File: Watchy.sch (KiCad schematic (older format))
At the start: 55 parts, among them J1 FPC24(0.5MM), J2 Micro USB, J3 Battery, M1 Vibration_Motor, Q1 AO3400A, Q2 UMH3N, Q4 CJ2301, Q5 S8050, SW1 BTN, SW2 BTN, SW3 BTN, SW4 BTN, U1 ESP32-PICO-D4, U2 ME6211C33M5G-N, U3 CP2104, U4 BMA423, U5 TP4054, U6 DS3231MZ

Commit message: added body step & STL
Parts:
- C1, C10, C11, C14, C2, C5, C6, C7, C8, C9: footprint Capacitors_SMD:C_0603 -> Capacitor_SMD:C_0603_1608Metric
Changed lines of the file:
@@
 F 0 "C1" H 865 1305 50  0000 L CNN
 F 1 "100nF" H 865 1235 50  0000 L CNN
-F 2 "Capacitors_SMD:C_0603" H 793 1090 50  0001 C CNN
+F 2 "Capacitor_SMD:C_0603_1608Metric" H 793 1090 50  0001 C CNN
 F 3 "" H 755 1240 50  0001 C CNN
 	1    755  1240
@@
 F 0 "C11" H 4890 4960 50  0000 L CNN
 F 1 "100nF" H 4890 4760 50  0000 L CNN
-F 2 "Capacitors_SMD:C_0603" H 4903 4710 50  0001 C CNN
+F 2 "Capacitor_SMD:C_0603_1608Metric" H 4903 4710 50  0001 C CNN
 F 3 "" H 4865 4860 50  0001 C CNN
 	1    4865 4860
@@
 F 0 "C2" V 9480 1545 50  0000 C CNN
 F 1 "1uF/50V" V 9645 1355 50  0000 C CNN
-F 2 "Capacitors_SMD:C_0603" H 9558 1305 50  0001 C CNN
+F 2 "Capacitor_SMD:C_0603_1608Metric" H 9558 1305 50  0001 C CNN
 F 3 "~" H 9520 1455 50  0001 C CNN
 	1    9520 1455
@@
 F 0 "C6" V 9555 2840 50  0000 C CNN
 F 1 "1uF/50V" V 9520 2155 50  0000 C CNN
-F 2 "Capacitors_SMD:C_0603" H 9558 2605 50  0001 C CNN
+F 2 "Capacitor_SMD:C_0603_1608Metric" H 9558 2605 50  0001 C CNN
 F 3 "~" H 9520 2755 50  0001 C CNN
 	1    9520 2755
@@
 F 0 "C8" V 9555 3040 50  0000 C CNN
 F 1 "1uF/50V" V 9525 2355 50  0000 C CNN
-F 2 "Capacitors_SMD:C_0603" H 9558 2805 50  0001 C CNN
+F 2 "Capacitor_SMD:C_0603_1608Metric" H 9558 2805 50  0001 C CNN
 F 3 "~" H 9520 2955 50  0001 C CNN
 	1    9520 2955
@@
 F 0 "C9" V 9555 3240 50  0000 C CNN
 F 1 "1uF/50V" V 9520 2540 50  0000 C CNN
-F 2 "Capacitors_SMD:C_0603" H 9558 3005 50  0001 C CNN
+F 2 "Capacitor_SMD:C_0603_1608Metric" H 9558 3005 50  0001 C CNN
 F 3 "~" H 9520 3155 50  0001 C CNN
 	1    9520 3155
@@
 F 0 "C10" V 9560 3470 50  0000 C CNN
 F 1 "1uF/50V" V 9520 2740 50  0000 C CNN
-F 2 "Capacitors_SMD:C_0603" H 9558 3205 50  0001 C CNN
+F 2 "Capacitor_SMD:C_0603_1608Metric" H 9558 3205 50  0001 C CNN
 F 3 "~" H 9520 3355 50  0001 C CNN
 	1    9520 3355
@@
 F 0 "C7" H 10540 2801 50  0000 L CNN
 F 1 "1uF/50V" H 10540 2710 50  0000 L CNN
-F 2 "Capacitors_SMD:C_0603" H 10463 2605 50  0001 C CNN
+F 2 "Capacitor_SMD:C_0603_1608Metric" H 10463 2605 50  0001 C CNN
 F 3 "~" H 10425 2755 50  0001 C CNN
 	1    10425 2755
@@
 F 0 "C5" H 7900 2060 50  0000 L CNN
 F 1 "1uF/50V" H 7900 1990 50  0000 L CNN
-F 2 "Capacitors_SMD:C_0603" H 7848 1920 50  0001 C CNN
+F 2 "Capacitor_SMD:C_0603_1608Metric" H 7848 1920 50  0001 C CNN
 F 3 "~" H 7810 2070 50  0001 C CNN
 	1    7810 2070
@@
 F 0 "C14" H 5735 7100 50  0000 L CNN
 F 1 "100nF" H 5860 6915 50  0000 L CNN
-F 2 "Capacitors_SMD:C_0603" H 5873 6870 50  0001 C CNN
+F 2 "Capacitor_SMD:C_0603_1608Metric" H 5873 6870 50  0001 C CNN
 F 3 "~" H 5835 7020 50  0001 C CNN
 	1    5835 7020

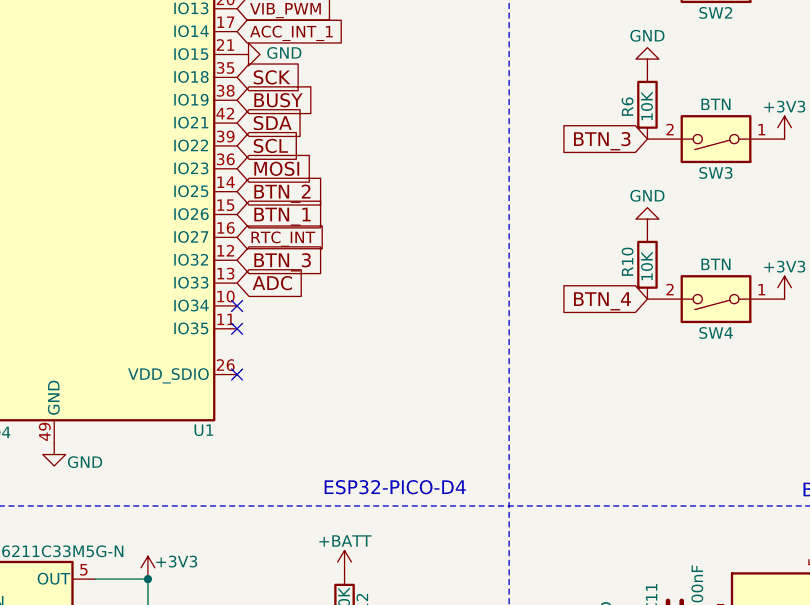
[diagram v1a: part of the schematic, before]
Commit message: added testpoints
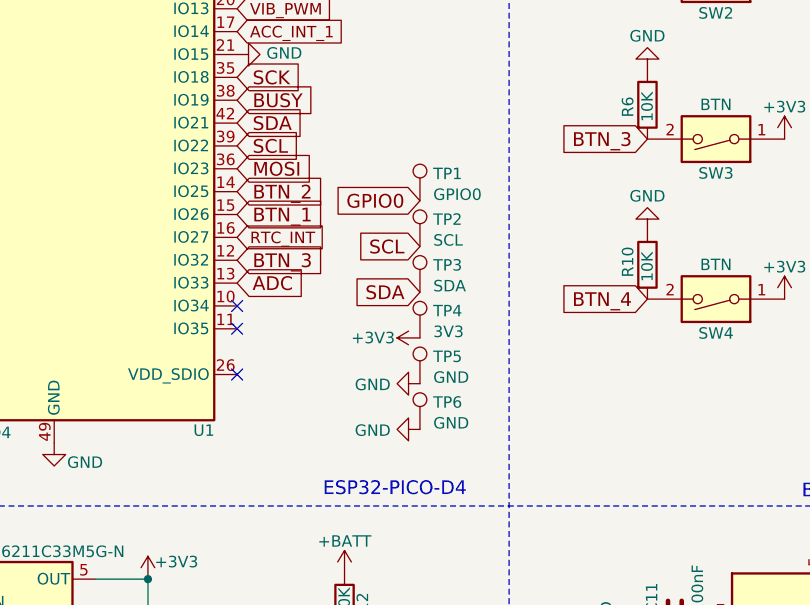
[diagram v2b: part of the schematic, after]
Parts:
- added TP1: GPIO0, TestPoint:TestPoint_Pad_D1.0mm, symbol Connector:TestPoint
- added TP2: SCL, TestPoint:TestPoint_Pad_D1.0mm, symbol Connector:TestPoint
- added TP3: SDA, TestPoint:TestPoint_Pad_D1.0mm, symbol Connector:TestPoint
- added TP4: 3V3, TestPoint:TestPoint_Pad_D1.0mm, symbol Connector:TestPoint
- added TP5, TP6: GND, TestPoint:TestPoint_Pad_D1.0mm, symbol Connector:TestPoint
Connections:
- net +3V3: now also TP4.1
- net GND: now also TP5.1, TP6.1
- net GPIO0: now also TP1.1
- net SCL: now also TP2.1
- net SDA: now also TP3.1
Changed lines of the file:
@@
 Wire Wire Line
 	9670 3255 9225 3255
+$Comp
+L Connector:TestPoint TP1
+U 1 1 60664F25
+P 3750 3030
+F 0 "TP1" H 3808 3148 50  0000 L CNN
+F 1 "GPIO0" H 3808 3057 50  0000 L CNN
+F 2 "TestPoint:TestPoint_Pad_D1.0mm" H 3950 3030 50  0001 C CNN
+F 3 "~" H 3950 3030 50  0001 C CNN
+	1    3750 3030
+	1    0    0    -1
+$EndComp
+$Comp
+L Connector:TestPoint TP2
+U 1 1 606661C8
+P 3750 3230
+F 0 "TP2" H 3808 3348 50  0000 L CNN
+F 1 "SCL" H 3808 3257 50  0000 L CNN
+F 2 "TestPoint:TestPoint_Pad_D1.0mm" H 3950 3230 50  0001 C CNN
+F 3 "~" H 3950 3230 50  0001 C CNN
+	1    3750 3230
+	1    0    0    -1
+$EndComp
+$Comp
+L Connector:TestPoint TP3
+U 1 1 60667C57
+P 3750 3430
+F 0 "TP3" H 3808 3548 50  0000 L CNN
+F 1 "SDA" H 3808 3457 50  0000 L CNN
+F 2 "TestPoint:TestPoint_Pad_D1.0mm" H 3950 3430 50  0001 C CNN
+F 3 "~" H 3950 3430 50  0001 C CNN
+	1    3750 3430
+	1    0    0    -1
+$EndComp
+$Comp
+L Connector:TestPoint TP4
+U 1 1 60668E1C
+P 3750 3630
+F 0 "TP4" H 3808 3748 50  0000 L CNN
+F 1 "3V3" H 3808 3657 50  0000 L CNN
+F 2 "TestPoint:TestPoint_Pad_D1.0mm" H 3950 3630 50  0001 C CNN
+F 3 "~" H 3950 3630 50  0001 C CNN
+	1    3750 3630
+	1    0    0    -1
+$EndComp
+$Comp
+L Connector:TestPoint TP5
+U 1 1 60669476
+P 3750 3830
+F 0 "TP5" H 3808 3948 50  0000 L CNN
+F 1 "GND" H 3808 3857 50  0000 L CNN
+F 2 "TestPoint:TestPoint_Pad_D1.0mm" H 3950 3830 50  0001 C CNN
+F 3 "~" H 3950 3830 50  0001 C CNN
+	1    3750 3830
+	1    0    0    -1
+$EndComp
+Text GLabel 3750 3030 0    60   Input ~ 0
+GPIO0
+Text GLabel 3750 3230 0    60   Input ~ 0
+SCL
+Text GLabel 3750 3430 0    60   Input ~ 0
+SDA
+$Comp
+L power:+3V3 #PWR0106
+U 1 1 60672CCA
+P 3750 3630
+F 0 "#PWR0106" H 3750 3480 50  0001 C CNN
+F 1 "+3V3" V 3750 3835 50  0000 C CNN
+F 2 "" H 3750 3630 50  0001 C CNN
+F 3 "" H 3750 3630 50  0001 C CNN
+	1    3750 3630
+	0    -1   -1   0
+$EndComp
+$Comp
+L power:GND #PWR0107
+U 1 1 60673AED
+P 3750 3830
+F 0 "#PWR0107" H 3750 3580 50  0001 C CNN
+F 1 "GND" V 3755 3702 50  0000 R CNN
+F 2 "" H 3750 3830 50  0001 C CNN
+F 3 "" H 3750 3830 50  0001 C CNN
+	1    3750 3830
+	0    1    1    0
+$EndComp
+$Comp
+L Connector:TestPoint TP6
+U 1 1 60739E66
+P 3750 4030
+F 0 "TP6" H 3808 4148 50  0000 L CNN
+F 1 "GND" H 3808 4057 50  0000 L CNN
+F 2 "TestPoint:TestPoint_Pad_D1.0mm" H 3950 4030 50  0001 C CNN
+F 3 "~" H 3950 4030 50  0001 C CNN
+	1    3750 4030
+	1    0    0    -1
+$EndComp
+$Comp
+L power:GND #PWR049
+U 1 1 6073A920
+P 3750 4030
+F 0 "#PWR049" H 3750 3780 50  0001 C CNN
+F 1 "GND" V 3755 3902 50  0000 R CNN
+F 2 "" H 3750 4030 50  0001 C CNN
+F 3 "" H 3750 4030 50  0001 C CNN
+	1    3750 4030
+	0    1    1    0
+$EndComp
 $EndSCHEMATC

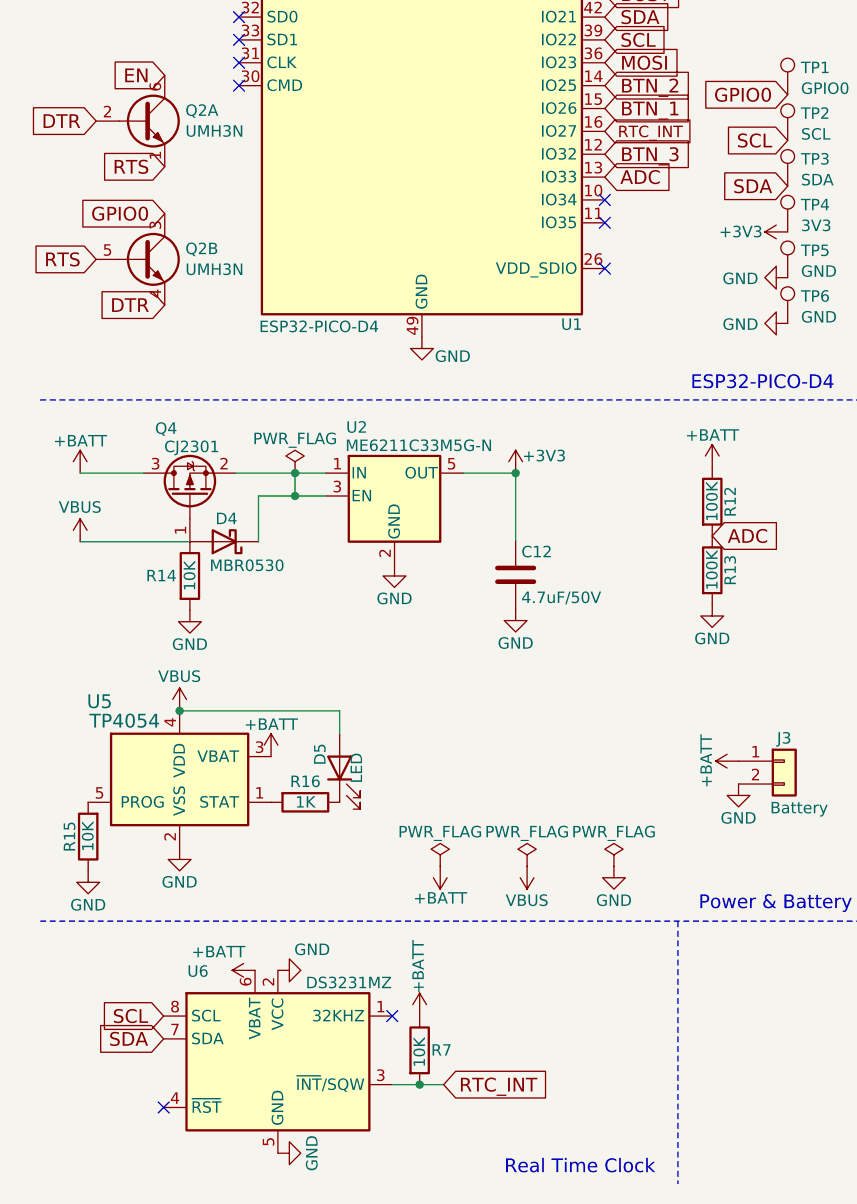
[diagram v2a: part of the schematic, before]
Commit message: v1.5
- switched to new RTC (PCF8563)
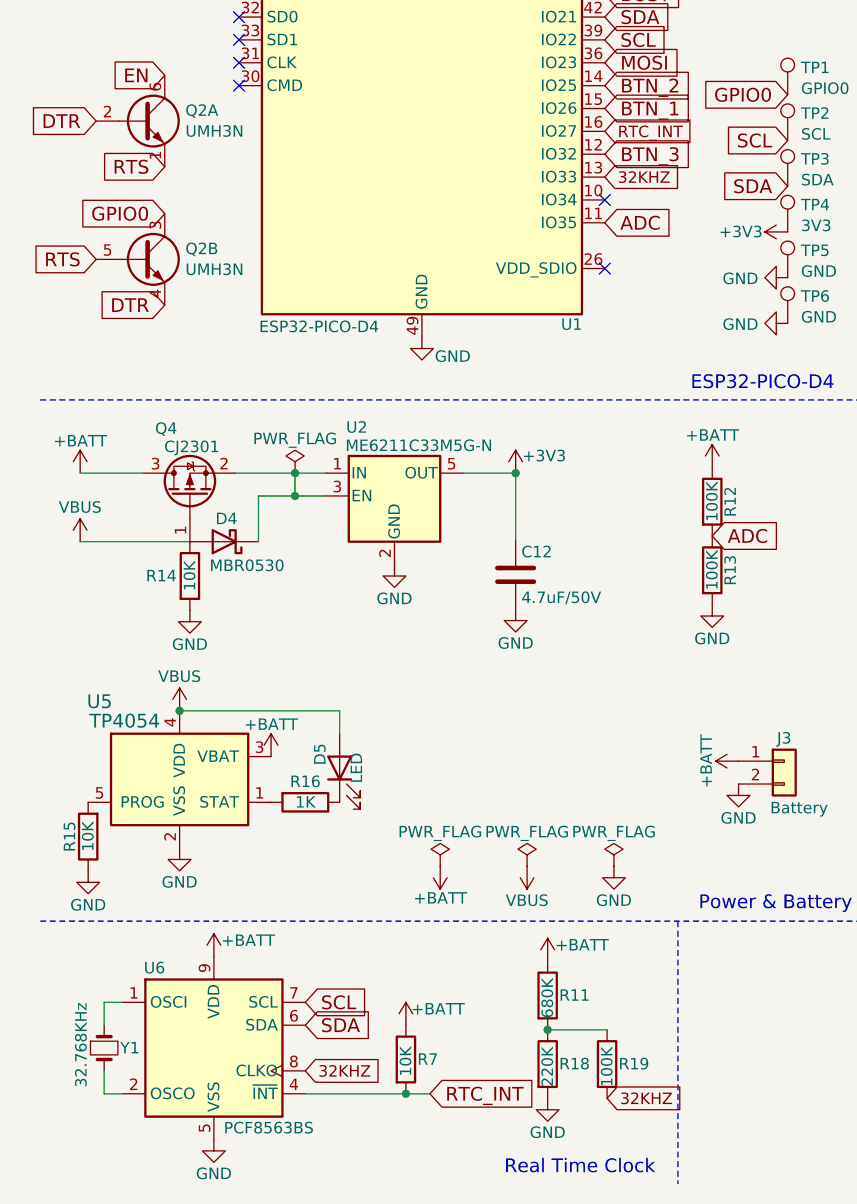
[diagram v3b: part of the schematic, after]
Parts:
- removed U6: DS3231MZ, Housings_SOIC:SOIC-8_3.9x4.9mm_Pitch1.27mm, symbol Timer_RTC:DS3231MZ
- added R11: 680K, Watchy:R_0402, symbol Device:R
- added R18: 220K, Watchy:R_0402, symbol Device:R
- added R19: 100K, Watchy:R_0402, symbol Device:R
- added U6: PCF8563BS, Package_DFN_QFN:DFN-10-1EP_3x3mm_P0.5mm_EP1.7x2.5mm, symbol Watchy:PCF8563BS
- added Y1: 32.768KHz, Crystal:Crystal_SMD_3215-2Pin_3.2x1.5mm, symbol Device:Crystal_Small
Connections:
- net +BATT: now also R11.1, U6.9 (VDD)
- net ADC: now also U1.11 (IO35); no longer U1.13 (IO33)
- net GND: now also R18.2, U6.5 (VSS)
- net RTC_INT: now also U6.4 (~INT~)
- net SCL: now also U6.7 (SCL)
- net SDA: now also U6.6 (SDA)
- new net: U6.1 (OSCI), Y1.1
- new net: U6.2 (OSCO), Y1.2
- new net: R11.2, R18.1, R19.1
- new net 32KHZ: R19.2, U1.13 (IO33), U6.8 (CLKO)
- no-connect marks 40 -> 37
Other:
- moved on the sheet: R7
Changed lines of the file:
@@
 NoConn ~ 6415 6160
 NoConn ~ 5915 4560
-Text GLabel 2245 7360 2    60   Input ~ 0
+Text GLabel 2185 7400 2    60   Input ~ 0
 RTC_INT
-Text GLabel 1020 7160 0    60   Input ~ 0
+Text GLabel 1640 7100 2    60   Input ~ 0
 SDA
 Text Notes 3325 4330 0    60   ~ 0
@@
 Text GLabel 4745 3460 0    60   Input ~ 0
 BTN_4
-Text GLabel 1020 7060 0    60   Input ~ 0
+Text GLabel 1640 7000 2    60   Input ~ 0
 SCL
 $Comp
 L power:GND #PWR064
 U 1 1 5B7B5EFD
-P 1520 7660
-F 0 "#PWR064" H 1520 7410 50  0001 C CNN
-F 1 "GND" H 1520 7510 50  0000 C CNN
-F 2 "" H 1520 7660 50  0001 C CNN
-F 3 "" H 1520 7660 50  0001 C CNN
-	1    1520 7660
-	0    -1   -1   0
+P 1240 7600
+F 0 "#PWR064" H 1240 7350 50  0001 C CNN
+F 1 "GND" H 1240 7450 50  0000 C CNN
+F 2 "" H 1240 7600 50  0001 C CNN
+F 3 "" H 1240 7600 50  0001 C CNN
+	1    1240 7600
+	1    0    0    -1
 $EndComp
 $Comp
 L power:+BATT #PWR061
 U 1 1 5D2D93AF
-P 1420 6860
-F 0 "#PWR061" H 1420 6710 50  0001 C CNN
-F 1 "+BATT" V 1500 7020 50  0000 C CNN
-F 2 "" H 1420 6860 50  0001 C CNN
-F 3 "" H 1420 6860 50  0001 C CNN
-	1    1420 6860
-	0    -1   -1   0
+P 1240 6800
+F 0 "#PWR061" H 1240 6650 50  0001 C CNN
+F 1 "+BATT" H 1390 6870 50  0000 C CNN
+F 2 "" H 1240 6800 50  0001 C CNN
+F 3 "" H 1240 6800 50  0001 C CNN
+	1    1240 6800
+	1    0    0    -1
 $EndComp
 $Comp
@@
 	0    -1   -1   0
 $EndComp
-NoConn ~ 1020 7460
-NoConn ~ 2020 7060
 $Comp
 L Watchy:BMA423 U4
@@
 NoConn ~ 1350 1490
 NoConn ~ 1350 1590
-NoConn ~ 2950 3590
 NoConn ~ 2950 3490
 Text GLabel 2950 1690 2    60   Input ~ 0
@@
 Text GLabel 2950 2990 2    60   Input ~ 0
 BTN_2
-Text GLabel 2950 3390 2    60   Input ~ 0
+Text GLabel 2950 3590 2    60   Input ~ 0
 ADC
-$Comp
-L Timer_RTC:DS3231MZ U6
-U 1 1 5EC01D20
-P 1520 7260
-F 0 "U6" H 1170 7655 50  0000 C CNN
-F 1 "DS3231MZ" H 1830 7605 50  0000 C CNN
-F 2 "Housings_SOIC:SOIC-8_3.9x4.9mm_Pitch1.27mm" H 1520 6760 50  0001 C CNN
-F 3 "http://datasheets.maximintegrated.com/en/ds/DS3231M.pdf" H 1520 6660 50  0001 C CNN
-	1    1520 7260
-	1    0    0    -1
-$EndComp
-$Comp
-L power:GND #PWR0101
-U 1 1 5EC052CA
-P 1520 6860
-F 0 "#PWR0101" H 1520 6610 50  0001 C CNN
-F 1 "GND" V 1610 6710 50  0000 C CNN
-F 2 "" H 1520 6860 50  0001 C CNN
-F 3 "" H 1520 6860 50  0001 C CNN
-	1    1520 6860
-	0    -1   -1   0
-$EndComp
 $Comp
 L Device:R R7
 U 1 1 5ECBDC05
-P 2140 7210
-F 0 "R7" H 2190 7210 50  0000 L CNN
-F 1 "10K" V 2140 7135 50  0000 L CNN
-F 2 "Resistors_SMD:R_0402" V 2070 7210 50  0001 C CNN
-F 3 "~" H 2140 7210 50  0001 C CNN
-	1    2140 7210
-	1    0    0    -1
-$EndComp
-Wire Wire Line
-	2020 7360 2140 7360
-Wire Wire Line
-	2140 7360 2245 7360
-Connection ~ 2140 7360
+P 2080 7250
+F 0 "R7" H 2130 7250 50  0000 L CNN
+F 1 "10K" V 2080 7175 50  0000 L CNN
+F 2 "Resistors_SMD:R_0402" V 2010 7250 50  0001 C CNN
+F 3 "~" H 2080 7250 50  0001 C CNN
+	1    2080 7250
+	1    0    0    -1
+$EndComp
+Wire Wire Line
+	2080 7400 2185 7400
+Connection ~ 2080 7400
 $Comp
 L power:+BATT #PWR0102
 U 1 1 5ECC1DD5
-P 2140 7060
-F 0 "#PWR0102" H 2140 6910 50  0001 C CNN
-F 1 "+BATT" V 2135 7275 50  0000 C CNN
-F 2 "" H 2140 7060 50  0001 C CNN
-F 3 "" H 2140 7060 50  0001 C CNN
-	1    2140 7060
+P 2080 7100
+F 0 "#PWR0102" H 2080 6950 50  0001 C CNN
+F 1 "+BATT" H 2220 7170 50  0000 C CNN
+F 2 "" H 2080 7100 50  0001 C CNN
+F 3 "" H 2080 7100 50  0001 C CNN
+	1    2080 7100
 	1    0    0    -1
 $EndComp
@@
 	0    1    1    0
 $EndComp
+$Comp
+L Watchy:PCF8563BS U6
+U 1 1 60B08009
+P 1240 7200
+F 0 "U6" H 980 7550 50  0000 C CNN
+F 1 "PCF8563BS" H 1480 6850 50  0000 C CNN
+F 2 "Package_DFN_QFN:DFN-10-1EP_3x3mm_P0.5mm_EP1.7x2.5mm" H 1240 8150 50  0001 C CNN
+F 3 "" H 1240 7200 50  0001 C CNN
+	1    1240 7200
+	1    0    0    -1
+$EndComp
+Wire Wire Line
+	1640 7400 2080 7400
+Text GLabel 1640 7300 2    50   Input ~ 0
+32KHZ
+$Comp
+L Device:Crystal_Small Y1
+U 1 1 60B140F6
+P 760 7200
+F 0 "Y1" V 760 7270 50  0000 L CNN
+F 1 "32.768KHz" H 560 7100 50  0000 L CNN
+F 2 "Crystal:Crystal_SMD_3215-2Pin_3.2x1.5mm" H 760 7200 50  0001 C CNN
+F 3 "~" H 760 7200 50  0001 C CNN
+	1    760  7200
+	0    1    1    0
+$EndComp
+Wire Wire Line
+	760  7100 760  7000
+Wire Wire Line
+	760  7000 840  7000
+Wire Wire Line
+	760  7300 760  7400
+Wire Wire Line
+	760  7400 840  7400
+Text GLabel 2960 7420 2    50   Input ~ 0
+32KHZ
+Text GLabel 2950 3390 2    50   Input ~ 0
+32KHZ
+$Comp
+L Device:R R11
+U 1 1 60B1BC3E
+P 2700 6970
+F 0 "R11" H 2750 6970 50  0000 L CNN
+F 1 "680K" V 2700 6870 50  0000 L CNN
+F 2 "Watchy:R_0402" V 2630 6970 50  0001 C CNN
+F 3 "~" H 2700 6970 50  0001 C CNN
+	1    2700 6970
+	1    0    0    -1
+$EndComp
+$Comp
+L power:+BATT #PWR065
+U 1 1 60B1BFDF
+P 2700 6820
+F 0 "#PWR065" H 2700 6670 50  0001 C CNN
+F 1 "+BATT" H 2850 6890 50  0000 C CNN
+F 2 "" H 2700 6820 50  0001 C CNN
+F 3 "" H 2700 6820 50  0001 C CNN
+	1    2700 6820
+	1    0    0    -1
+$EndComp
+$Comp
+L Device:R R18
+U 1 1 60B20057
+P 2700 7270
+F 0 "R18" H 2750 7270 50  0000 L CNN
+F 1 "220K" V 2700 7170 50  0000 L CNN
+F 2 "Watchy:R_0402" V 2630 7270 50  0001 C CNN
+F 3 "~" H 2700 7270 50  0001 C CNN
+	1    2700 7270
+	1    0    0    -1
+$EndComp
+$Comp
+L power:GND #PWR066
+U 1 1 60B20503
+P 2700 7420
+F 0 "#PWR066" H 2700 7170 50  0001 C CNN
+F 1 "GND" H 2700 7270 50  0000 C CNN
+F 2 "" H 2700 7420 50  0001 C CNN
+F 3 "" H 2700 7420 50  0001 C CNN
+	1    2700 7420
+	1    0    0    -1
+$EndComp
+$Comp
+L Device:R R19
+U 1 1 60B235B4
+P 2960 7270
+F 0 "R19" H 3010 7270 50  0000 L CNN
+F 1 "100K" V 2960 7170 50  0000 L CNN
+F 2 "Watchy:R_0402" V 2890 7270 50  0001 C CNN
+F 3 "~" H 2960 7270 50  0001 C CNN
+	1    2960 7270
+	1    0    0    -1
+$EndComp
+Wire Wire Line
+	2960 7120 2700 7120
+Connection ~ 2700 7120
 $EndSCHEMATC

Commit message: label CP2102
CP2102
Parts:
- U3: value CP2104 -> CP2102
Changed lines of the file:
@@
 P 5715 5460
 F 0 "U3" H 6075 6425 50  0000 R CNN
-F 1 "CP2104" H 6280 6315 50  0000 R CNN
+F 1 "CP2102" H 6280 6315 50  0000 R CNN
 F 2 "Housings_DFN_QFN:QFN-24-1EP_4x4mm_Pitch0.5mm" H 5865 4510 50  0001 L CNN
 F 3 "" H 5165 6710 50  0001 C CNN

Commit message: v2.0
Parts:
- added C13: 4.7uF, Capacitor_SMD:C_0402_1005Metric, symbol Device:C
- added R20: 100K, Watchy:R_0402, symbol Device:R
- C11: value 100nF -> 4.7uF; footprint Capacitor_SMD:C_0603_1608Metric -> Capacitor_SMD:C_0402_1005Metric
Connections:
- net +3V3: now also R20.1
- net ADC: now also U1.10 (IO34); no longer U1.11 (IO35)
- net BTN_3: now also U1.11 (IO35); no longer U1.12 (IO32)
- net GND: now also C13.2
- net RES: now also R20.2
- net at U3.5 (VIO), U3.6 (VDD): now also C13.1
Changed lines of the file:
@@
 Title "Watchy"
 Date ""
-Rev "1.5"
+Rev "2.0"
 Comp ""
 Comment1 ""
@@
 P 4865 4860
 F 0 "C11" H 4890 4960 50  0000 L CNN
-F 1 "100nF" H 4890 4760 50  0000 L CNN
-F 2 "Capacitor_SMD:C_0603_1608Metric" H 4903 4710 50  0001 C CNN
+F 1 "4.7uF" H 4890 4760 50  0000 L CNN
+F 2 "Capacitor_SMD:C_0402_1005Metric" H 4903 4710 50  0001 C CNN
 F 3 "" H 4865 4860 50  0001 C CNN
 	1    4865 4860
@@
 NoConn ~ 8305 5035
 NoConn ~ 9705 5035
-Wire Wire Line
-	5515 4560 5715 4560
 Wire Notes Line
 	6970 6530 6970 4365
@@
 NoConn ~ 1350 1490
 NoConn ~ 1350 1590
-NoConn ~ 2950 3490
 Text GLabel 2950 1690 2    60   Input ~ 0
 BTN_4
@@
 Text GLabel 2950 2090 2    50   Input ~ 0
 ACC_INT_2
-Text GLabel 2950 3290 2    60   Input ~ 0
+Text GLabel 2950 3590 2    60   Input ~ 0
 BTN_3
 Text GLabel 2950 3190 2    50   Input ~ 0
@@
 Text GLabel 2950 2990 2    60   Input ~ 0
 BTN_2
-Text GLabel 2950 3590 2    60   Input ~ 0
+Text GLabel 2950 3490 2    60   Input ~ 0
 ADC
 $Comp
@@
 	2960 7120 2700 7120
 Connection ~ 2700 7120
+$Comp
+L Device:C C13
+U 1 1 61C6C07A
+P 4260 4560
+F 0 "C13" H 4285 4660 50  0000 L CNN
+F 1 "4.7uF" H 4285 4460 50  0000 L CNN
+F 2 "Capacitor_SMD:C_0402_1005Metric" H 4298 4410 50  0001 C CNN
+F 3 "" H 4260 4560 50  0001 C CNN
+	1    4260 4560
+	1    0    0    -1
+$EndComp
+Wire Wire Line
+	4810 4410 4810 4560
+Wire Wire Line
+	4810 4560 5515 4560
+Connection ~ 5515 4560
+Wire Wire Line
+	5515 4560 5715 4560
+$Comp
+L power:GND #PWR0101
+U 1 1 61C70501
+P 4260 4710
+F 0 "#PWR0101" H 4260 4460 50  0001 C CNN
+F 1 "GND" H 4390 4660 50  0000 C CNN
+F 2 "" H 4260 4710 50  0001 C CNN
+F 3 "" H 4260 4710 50  0001 C CNN
+	1    4260 4710
+	1    0    0    -1
+$EndComp
+Text GLabel 10400 1960 0    50   Input ~ 0
+RES
+$Comp
+L Device:R R20
+U 1 1 61C72728
+P 10400 1810
+F 0 "R20" V 10480 1810 50  0000 C CNN
+F 1 "100K" V 10400 1810 50  0000 C CNN
+F 2 "Watchy:R_0402" V 10330 1810 50  0001 C CNN
+F 3 "" H 10400 1810 50  0001 C CNN
+	1    10400 1810
+	1    0    0    -1
+$EndComp
+$Comp
+L power:+3.3V #PWR0108
+U 1 1 61C7317C
+P 10400 1660
+F 0 "#PWR0108" H 10400 1510 50  0001 C CNN
+F 1 "+3.3V" H 10265 1780 50  0000 C CNN
+F 2 "" H 10400 1660 50  0001 C CNN
+F 3 "" H 10400 1660 50  0001 C CNN
+	1    10400 1660
+	1    0    0    -1
+$EndComp
+NoConn ~ 2950 3290
+Wire Wire Line
+	4260 4410 4810 4410
 $EndSCHEMATC
